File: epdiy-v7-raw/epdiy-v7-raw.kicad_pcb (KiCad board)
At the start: 4 copper layers, 128.4 x 74.9 mm, 105 parts, among them CN1 WP27D-S050VA3-R15000, J1 USB_C_Receptacle_USB2.0, J2 EXTENSION_HEADER, J5 CONN_BAT, J7 ESP_HDR, Q1 AO3401A, SW1 TC-0522C-1.7-160G, SW2 TC-0522C-1.7-160G, U1 RT9080-33GJ5, U10 ED060XC5, U11 TP4056, U3 RSL48_4P4X4P4, U4 USBLC6-2P6, U8 ESP32-S3-WROOM-1, Y1 RV-3032-C7

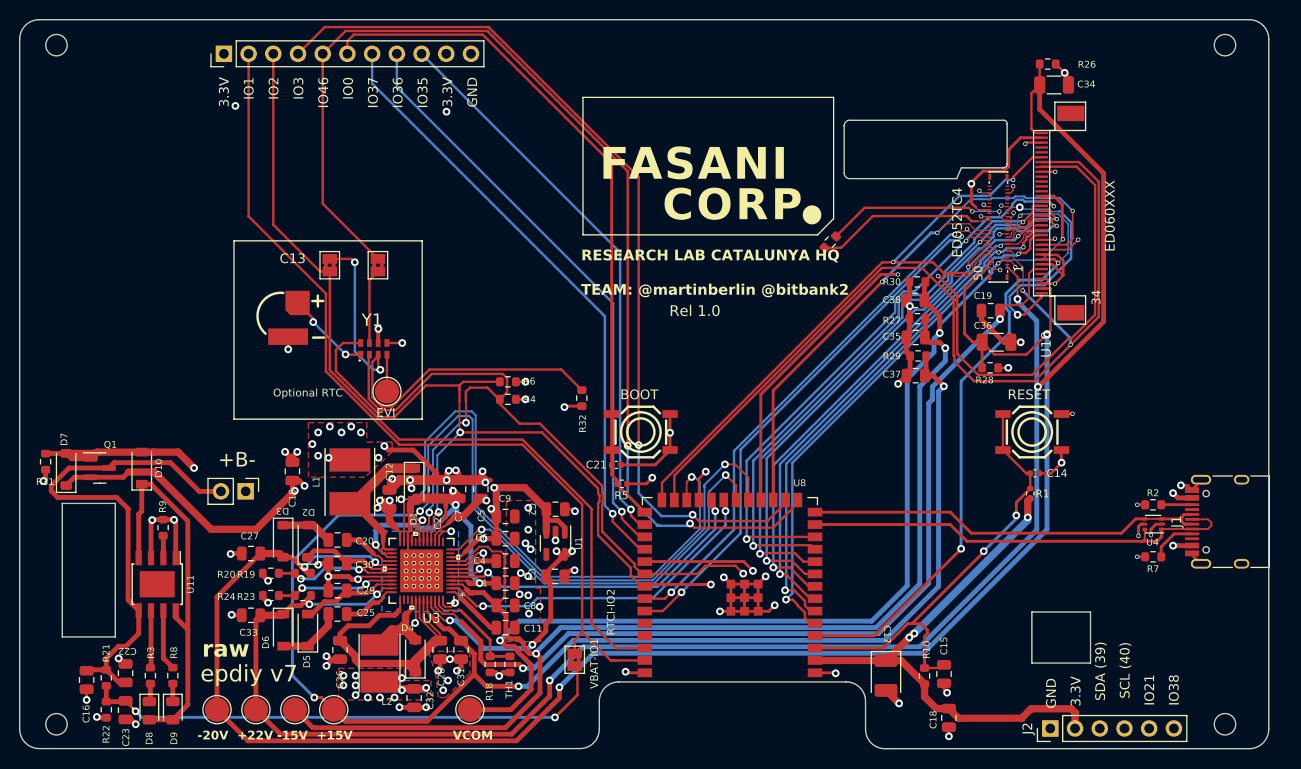
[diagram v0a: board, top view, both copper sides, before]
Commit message: Add signals test header
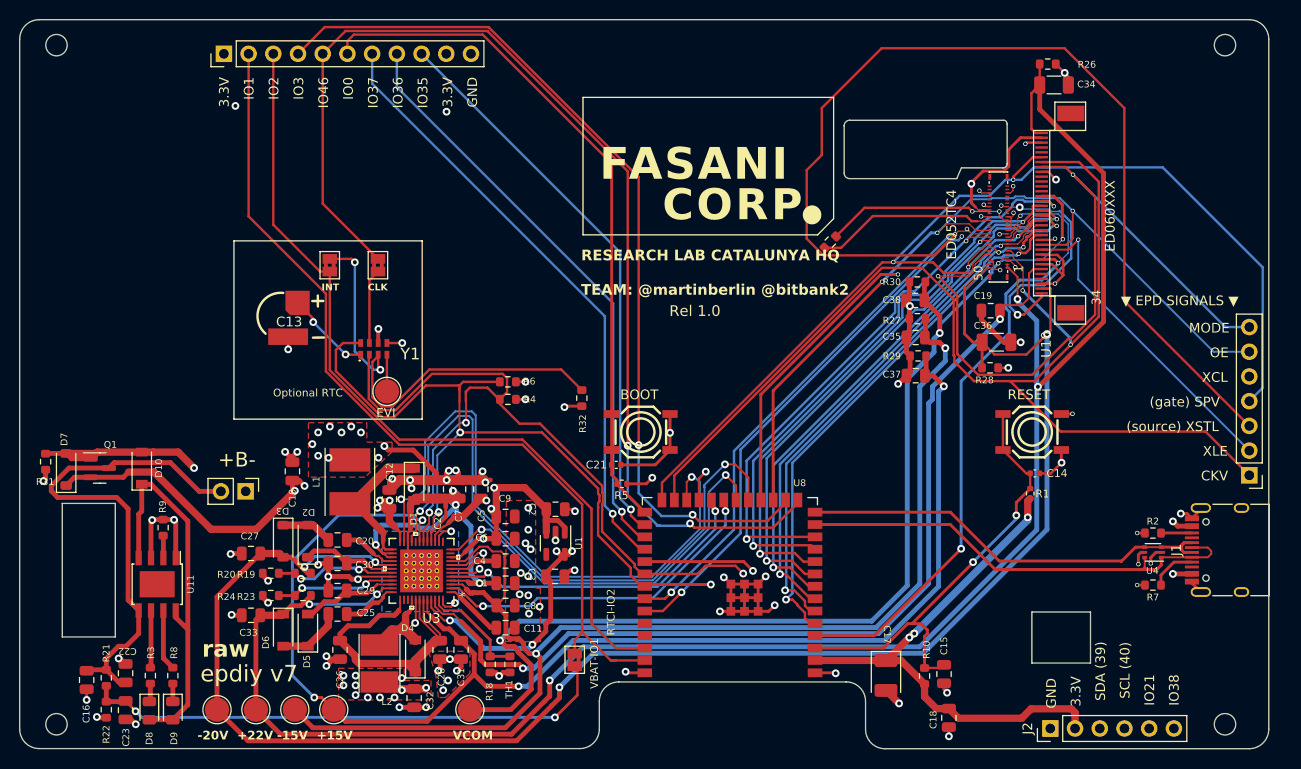
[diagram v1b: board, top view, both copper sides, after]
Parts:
- added J3: SIGNALS_HEADER, Connector_PinHeader_2.54mm:PinHeader_1x07_P2.54mm_Vertical, F.Cu at (184.4, 94.5)
- U3: value RSL48_4P4X4P4 -> TPS651851RSLR
- moved J1 2.91 mm to (182.5, 102.2)
- moved R2 2.91 mm to (174.5, 100.4)
- moved R7 2.91 mm to (174.5, 105.8)
- moved U4 2.91 mm to (174.5, 102.4)
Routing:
- net /XSTL: track 74.1 -> 179.2 mm
- net /EP_SPV: track 66.5 -> 111.2 mm
- net /XLE: track 81.9 -> 110.9 mm
- net /CKV: track 99.4 -> 128.0 mm
- net /XCL: track 67.8 -> 92.3 mm
- net /EP_OE: track 63.3 -> 87.4 mm
- net /EP_MODE: track 86.9 -> 110.8 mm, vias 2 -> 3
- net VBUS: track 161.8 -> 158.9 mm
- net /ESP_USB+: track 42.5 -> 43.7 mm
- net /ESP_USB-: track 46.5 -> 47.6 mm
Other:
- board text added: "(gate) SPV"
- board text added: "(source) XSTL"
- board text added: "CKV"
- board text added: "CLK"
- board text added: "INT"
- board text added: "MODE"
- board text added: "OE"
- board text added: "XCL"
- board text added: "XLE"
- board text added: "▼ EPD SIGNALS ▼"

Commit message: Update v7 raw
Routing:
- net /XSTL: track 179.2 -> 103.0 mm, vias 4 -> 5
- net GND: track 186.9 -> 188.4 mm, vias 96 -> 95
- net EPD_VDD: track 129.1 -> 129.6 mm

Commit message: Add 6 in. connector 1mm carving
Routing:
- net /EP_SPV: track 111.2 -> 108.2 mm
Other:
- outline, holes or cut-outs redrawn
- board text added: "RESEARCH LAB CATALUNYA HQ https://github.com/bitbank2/FastEPD TEAM: @martinberlin @bitbank2"
- board text added: "based in epdiy v7 by Valentin Roland 2023 Thanks to all the contributors! For sources and documentation visit https://github.com/bitbank2/FastEPD"
- board text removed: "RESEARCH LAB CATALUNYA HQ TEAM: @martinberlin @bitbank2"
- board text removed: "Rel 1.1.1 PCB custom modified for 9.7, 13.3 inch displays (8 bit)"
- board text removed: "epdiy v7 by Valentin Roland 2023 Thanks to the epdiy contributors! For sources and documentation visit https://github.com/vroland/epdiy"
